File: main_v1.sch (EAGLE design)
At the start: 41 parts, among them IC1 MEGA8-P, IC2 7805TV

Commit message: Prettify
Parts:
- removed GOLD_ORB_SM2: OSHWLOGO_GOLD_ORB_MED, bfl:OSHWLOGO_GOLD_ORB_MED
- removed GOLD_ORB_SM3: OSHWLOGO_GOLD_ORB_SM, bfl:OSHWLOGO_GOLD_ORB_SM
- renumbered SV1 to H1, SV2 to H2, SV3 to H3, SV4 to H4, U$1 to IC5, U$2 to IC6, U$3 to IC4

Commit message: Added better OSHW logo
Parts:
- removed GOLD_ORB_SM1: OSHWLOGO_GOLD_ORB_LG, bfl:OSHWLOGO_GOLD_ORB_LG
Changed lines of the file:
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@@
 <part name="C8" library="adafruit" deviceset="CPOL-US" device="E2.5-5"/>
 <part name="GND22" library="supply1" deviceset="GND" device=""/>
-<part name="GOLD_ORB_SM1" library="bfl" deviceset="OSHWLOGO" device="_GOLD_ORB_LG"/>
 <part name="IC2" library="linear" deviceset="78*" device="TV" technology="05"/>
 <part name="GND9" library="supply1" deviceset="GND" device=""/>
@@
 <instance part="C8" gate="G$1" x="238.76" y="335.28"/>
 <instance part="GND22" gate="1" x="238.76" y="325.12"/>
-<instance part="GOLD_ORB_SM1" gate="G$1" x="48.26" y="73.66"/>
 <instance part="IC2" gate="A1" x="-17.78" y="88.9"/>
 <instance part="GND9" gate="1" x="-17.78" y="66.04"/>

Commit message: Prepare to move the atmega
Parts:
- added ESP8266: (no value), adafruit:PINHD-2X4
- added ICSP2: (no value), con-lstb:MA05-1
- added R13, R14, R15, R16, R17: (no value), resistor:R-EU_0204/7
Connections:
- new net N$10: ESP8266.1, ICSP2.1
- new net N$12: ESP8266.7, ICSP2.5, R17.2
- new net N$14: ESP8266.8, ICSP2.2
- new net N$17: ESP8266.3, R14.2
- new net N$19: ESP8266.5, R13.2
- new net SCL: ESP8266.4, IC1.PC5(ADC5/SCL), R16.2
- new net SDA: ESP8266.6, IC1.PC4(ADC4/SDA), ICSP2.4, R15.2
- net GND: now also ESP8266.2, ICSP2.3
- net VCC: now also R13.1, R14.1, R15.1, R16.1, R17.1
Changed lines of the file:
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@@
 <part name="R11" library="resistor" deviceset="R-EU_" device="0204/7"/>
 <part name="R12" library="resistor" deviceset="R-EU_" device="0204/7"/>
+<part name="R13" library="resistor" deviceset="R-EU_" device="0204/7"/>
+<part name="R14" library="resistor" deviceset="R-EU_" device="0204/7"/>
+<part name="R15" library="resistor" deviceset="R-EU_" device="0204/7"/>
+<part name="P+6" library="supply1" deviceset="VCC" device=""/>
+<part name="GND8" library="supply1" deviceset="GND" device=""/>
+<part name="R16" library="resistor" deviceset="R-EU_" device="0204/7"/>
+<part name="ICSP2" library="con-lstb" deviceset="MA05-1" device=""/>
+<part name="ESP8266" library="adafruit" deviceset="PINHD-2X4" device=""/>
+<part name="R17" library="resistor" deviceset="R-EU_" device="0204/7"/>
 </parts>
 <sheets>
@@
 <instance part="R11" gate="G$1" x="63.5" y="365.76" rot="R180"/>
 <instance part="R12" gate="G$1" x="63.5" y="370.84" rot="R180"/>
+<instance part="R13" gate="G$1" x="-144.78" y="294.64" rot="R270"/>
+<instance part="R14" gate="G$1" x="-137.16" y="294.64" rot="R270"/>
+<instance part="R15" gate="G$1" x="-81.28" y="294.64" rot="R270"/>
+<instance part="P+6" gate="VCC" x="-129.54" y="320.04"/>
+<instance part="GND8" gate="1" x="-114.3" y="208.28"/>
+<instance part="R16" gate="G$1" x="-86.36" y="294.64" rot="R270"/>
+<instance part="ICSP2" gate="G$1" x="-63.5" y="248.92" rot="R180"/>
+<instance part="ESP8266" gate="A" x="-116.84" y="271.78"/>
+<instance part="R17" gate="G$1" x="-129.54" y="294.64" rot="R270"/>
 </instances>
 <busses>
@@
 <wire x1="160.02" y1="88.9" x2="195.58" y2="88.9" width="0.762" layer="92"/>
 <wire x1="195.58" y1="88.9" x2="195.58" y2="233.68" width="0.762" layer="92"/>
-<wire x1="160.02" y1="88.9" x2="160.02" y2="281.94" width="0.762" layer="92"/>
+<wire x1="160.02" y1="88.9" x2="160.02" y2="236.22" width="0.762" layer="92"/>
 </segment>
 </bus>
@@
 <wire x1="38.1" y1="358.14" x2="38.1" y2="337.82" width="0.1524" layer="91"/>
 </segment>
+<segment>
+<pinref part="ICSP2" gate="G$1" pin="3"/>
+<wire x1="-71.12" y1="248.92" x2="-101.6" y2="248.92" width="0.1524" layer="91"/>
+<pinref part="GND8" gate="1" pin="GND"/>
+<wire x1="-101.6" y1="248.92" x2="-114.3" y2="248.92" width="0.1524" layer="91"/>
+<wire x1="-114.3" y1="248.92" x2="-114.3" y2="210.82" width="0.1524" layer="91"/>
+<pinref part="ESP8266" gate="A" pin="2"/>
+<wire x1="-111.76" y1="276.86" x2="-101.6" y2="276.86" width="0.1524" layer="91"/>
+<wire x1="-101.6" y1="276.86" x2="-101.6" y2="248.92" width="0.1524" layer="91"/>
+<junction x="-101.6" y="248.92"/>
+</segment>
 </net>
 <net name="VCC" class="0">
@@
 <wire x1="40.64" y1="353.06" x2="40.64" y2="365.76" width="0.1524" layer="91"/>
 <wire x1="40.64" y1="365.76" x2="17.78" y2="365.76" width="0.1524" layer="91"/>
+</segment>
+<segment>
+<pinref part="P+6" gate="VCC" pin="VCC"/>
+<pinref part="R15" gate="G$1" pin="1"/>
+<wire x1="-129.54" y1="312.42" x2="-129.54" y2="317.5" width="0.1524" layer="91"/>
+<wire x1="-81.28" y1="299.72" x2="-81.28" y2="312.42" width="0.1524" layer="91"/>
+<wire x1="-81.28" y1="312.42" x2="-86.36" y2="312.42" width="0.1524" layer="91"/>
+<pinref part="R16" gate="G$1" pin="1"/>
+<wire x1="-86.36" y1="312.42" x2="-129.54" y2="312.42" width="0.1524" layer="91"/>
+<wire x1="-86.36" y1="299.72" x2="-86.36" y2="312.42" width="0.1524" layer="91"/>
+<junction x="-86.36" y="312.42"/>
+<pinref part="R14" gate="G$1" pin="1"/>
+<wire x1="-137.16" y1="299.72" x2="-137.16" y2="312.42" width="0.1524" layer="91"/>
+<wire x1="-137.16" y1="312.42" x2="-129.54" y2="312.42" width="0.1524" layer="91"/>
+<junction x="-129.54" y="312.42"/>
+<pinref part="R13" gate="G$1" pin="1"/>
+<wire x1="-144.78" y1="299.72" x2="-144.78" y2="312.42" width="0.1524" layer="91"/>
+<wire x1="-144.78" y1="312.42" x2="-137.16" y2="312.42" width="0.1524" layer="91"/>
+<junction x="-137.16" y="312.42"/>
+<pinref part="R17" gate="G$1" pin="1"/>
+<wire x1="-129.54" y1="299.72" x2="-129.54" y2="312.42" width="0.1524" layer="91"/>
 </segment>
 </net>
@@
 </segment>
 </net>
+<net name="SCL" class="0">
+<segment>
+<pinref part="R16" gate="G$1" pin="2"/>
+<pinref part="ESP8266" gate="A" pin="4"/>
+<wire x1="-111.76" y1="274.32" x2="-86.36" y2="274.32" width="0.1524" layer="91"/>
+<wire x1="-86.36" y1="274.32" x2="-86.36" y2="289.56" width="0.1524" layer="91"/>
+<label x="-76.2" y="274.32" size="1.778" layer="95"/>
+<wire x1="-86.36" y1="274.32" x2="-78.74" y2="274.32" width="0.1524" layer="91"/>
+<junction x="-86.36" y="274.32"/>
+</segment>
+<segment>
+<pinref part="IC1" gate="G$1" pin="PC5(ADC5/SCL)"/>
+<wire x1="33.02" y1="213.36" x2="38.1" y2="213.36" width="0.1524" layer="91"/>
+<label x="38.1" y="213.36" size="1.778" layer="95"/>
+</segment>
+</net>
+<net name="N$10" class="0">
+<segment>
+<pinref part="ESP8266" gate="A" pin="1"/>
+<wire x1="-119.38" y1="276.86" x2="-132.08" y2="276.86" width="0.1524" layer="91"/>
+<pinref part="ICSP2" gate="G$1" pin="1"/>
+<wire x1="-132.08" y1="276.86" x2="-132.08" y2="254" width="0.1524" layer="91"/>
+<wire x1="-132.08" y1="254" x2="-71.12" y2="254" width="0.1524" layer="91"/>
+</segment>
+</net>
+<net name="N$14" class="0">
+<segment>
+<pinref part="ESP8266" gate="A" pin="8"/>
+<wire x1="-111.76" y1="269.24" x2="-99.06" y2="269.24" width="0.1524" layer="91"/>
+<pinref part="ICSP2" gate="G$1" pin="2"/>
+<wire x1="-99.06" y1="269.24" x2="-99.06" y2="251.46" width="0.1524" layer="91"/>
+<wire x1="-99.06" y1="251.46" x2="-71.12" y2="251.46" width="0.1524" layer="91"/>
+</segment>
+</net>
+<net name="N$17" class="0">
+<segment>
+<pinref part="ESP8266" gate="A" pin="3"/>
+<pinref part="R14" gate="G$1" pin="2"/>
+<wire x1="-119.38" y1="274.32" x2="-137.16" y2="274.32" width="0.1524" layer="91"/>
+<wire x1="-137.16" y1="274.32" x2="-137.16" y2="289.56" width="0.1524" layer="91"/>
+</segment>
+</net>
+<net name="N$19" class="0">
+<segment>
+<pinref part="ESP8266" gate="A" pin="5"/>
+<pinref part="R13" gate="G$1" pin="2"/>
+<wire x1="-119.38" y1="271.78" x2="-144.78" y2="271.78" width="0.1524" layer="91"/>
+<wire x1="-144.78" y1="271.78" x2="-144.78" y2="289.56" width="0.1524" layer="91"/>
+</segment>
+</net>
+<net name="SDA" class="0">
+<segment>
+<pinref part="R15" gate="G$1" pin="2"/>
+<pinref part="ESP8266" gate="A" pin="6"/>
+<wire x1="-81.28" y1="289.56" x2="-81.28" y2="271.78" width="0.1524" layer="91"/>
+<wire x1="-81.28" y1="271.78" x2="-96.52" y2="271.78" width="0.1524" layer="91"/>
+<wire x1="-96.52" y1="271.78" x2="-111.76" y2="271.78" width="0.1524" layer="91"/>
+<junction x="-96.52" y="271.78"/>
+<label x="-76.2" y="271.78" size="1.778" layer="95"/>
+<wire x1="-96.52" y1="246.38" x2="-96.52" y2="271.78" width="0.1524" layer="91"/>
+<wire x1="-81.28" y1="271.78" x2="-78.74" y2="271.78" width="0.1524" layer="91"/>
+<junction x="-81.28" y="271.78"/>
+<pinref part="ICSP2" gate="G$1" pin="4"/>
+<wire x1="-71.12" y1="246.38" x2="-96.52" y2="246.38" width="0.1524" layer="91"/>
+</segment>
+<segment>
+<pinref part="IC1" gate="G$1" pin="PC4(ADC4/SDA)"/>
+<wire x1="33.02" y1="215.9" x2="38.1" y2="215.9" width="0.1524" layer="91"/>
+<label x="38.1" y="215.9" size="1.778" layer="95"/>
+</segment>
+</net>
+<net name="N$12" class="0">
+<segment>
+<pinref part="ESP8266" gate="A" pin="7"/>
+<wire x1="-119.38" y1="269.24" x2="-129.54" y2="269.24" width="0.1524" layer="91"/>
+<wire x1="-129.54" y1="243.84" x2="-129.54" y2="269.24" width="0.1524" layer="91"/>
+<pinref part="R17" gate="G$1" pin="2"/>
+<wire x1="-129.54" y1="289.56" x2="-129.54" y2="269.24" width="0.1524" layer="91"/>
+<junction x="-129.54" y="269.24"/>
+<pinref part="ICSP2" gate="G$1" pin="5"/>
+<wire x1="-71.12" y1="243.84" x2="-129.54" y2="243.84" width="0.1524" layer="91"/>
+</segment>
+</net>

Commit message: Move ESP ICSP header, and bits into the board
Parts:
- R13, R15, R17: device resistor:R-EU_0204/7 -> resistor:R-EU_0204/2V
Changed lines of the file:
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@@
 <part name="R11" library="resistor" deviceset="R-EU_" device="0204/7"/>
 <part name="R12" library="resistor" deviceset="R-EU_" device="0204/7"/>
-<part name="R13" library="resistor" deviceset="R-EU_" device="0204/7"/>
+<part name="R13" library="resistor" deviceset="R-EU_" device="0204/2V"/>
 <part name="R14" library="resistor" deviceset="R-EU_" device="0204/7"/>
-<part name="R15" library="resistor" deviceset="R-EU_" device="0204/7"/>
+<part name="R15" library="resistor" deviceset="R-EU_" device="0204/2V"/>
 <part name="P+6" library="supply1" deviceset="VCC" device=""/>
 <part name="GND8" library="supply1" deviceset="GND" device=""/>
@@
 <part name="ICSP2" library="con-lstb" deviceset="MA05-1" device=""/>
 <part name="ESP8266" library="adafruit" deviceset="PINHD-2X4" device=""/>
-<part name="R17" library="resistor" deviceset="R-EU_" device="0204/7"/>
+<part name="R17" library="resistor" deviceset="R-EU_" device="0204/2V"/>
 </parts>
 <sheets>

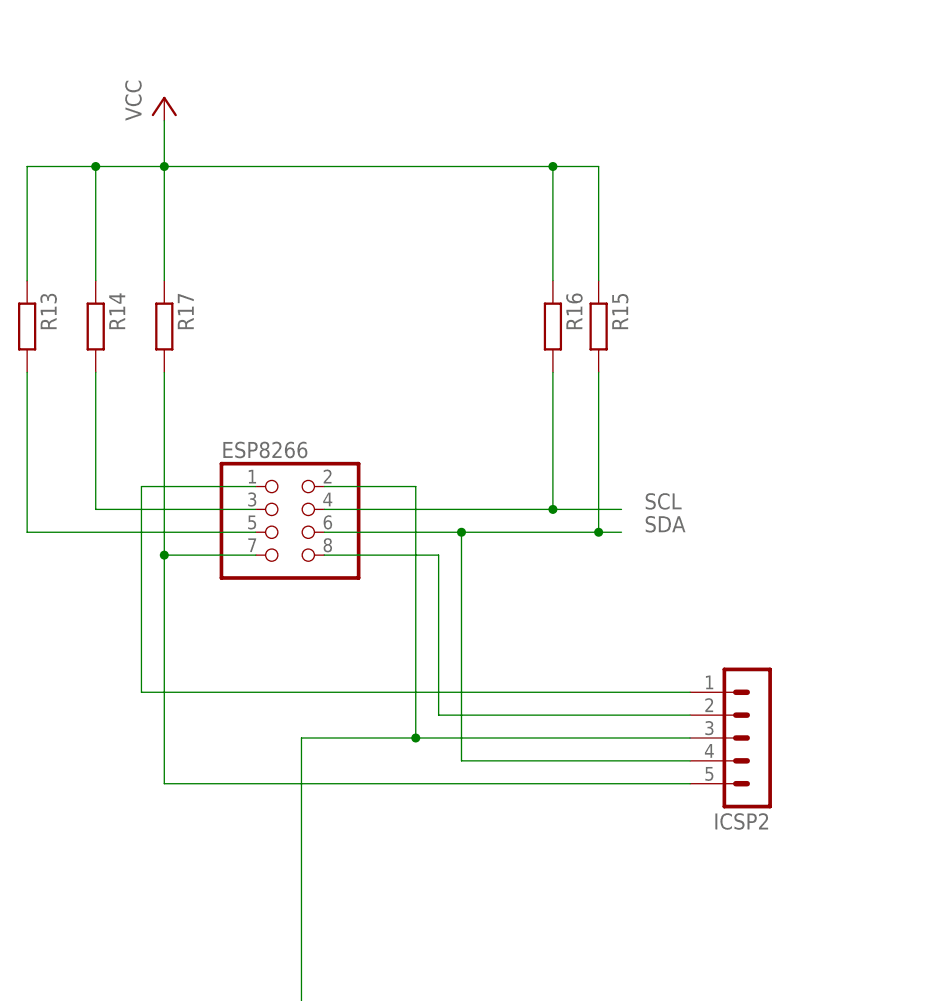
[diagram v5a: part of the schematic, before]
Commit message: Fix ESP socket connections
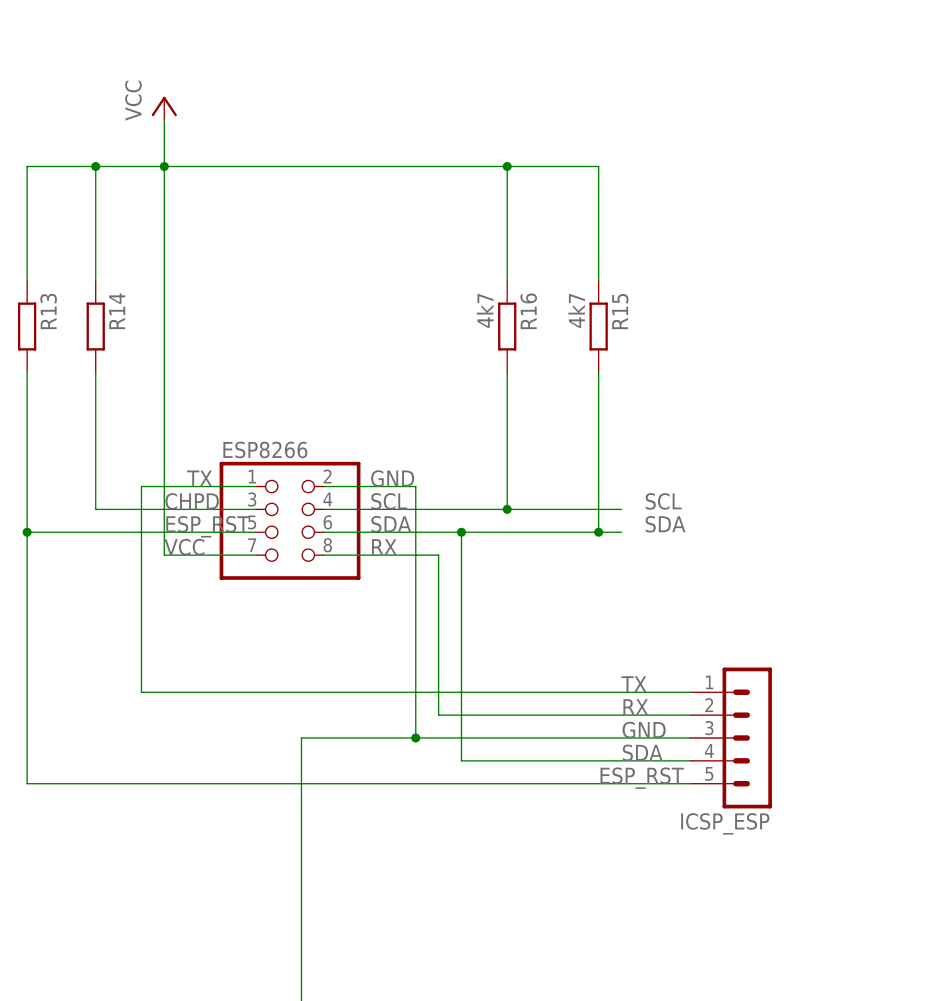
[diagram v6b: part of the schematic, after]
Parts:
- removed R17: (no value), resistor:R-EU_0204/2V
- R15: value (none) -> 4k7; device resistor:R-EU_0204/2V -> resistor:R-EU_0204/7
- R16: value (none) -> 4k7
- renumbered ICSP2 to ICSP_ESP
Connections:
- net N$10 renamed TX
- net N$14 renamed RX
- net N$17 renamed CHPD
- removed net N$12: ESP8266.7, ICSP_ESP.5, R17.2
- removed net N$19: ESP8266.5, R13.2
- new net ESP_RST: ESP8266.5, ICSP_ESP.5, R13.2
- net VCC: now also ESP8266.7; no longer R17.1
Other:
- moved on the sheet: R16
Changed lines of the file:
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@@
 <part name="R13" library="resistor" deviceset="R-EU_" device="0204/2V"/>
 <part name="R14" library="resistor" deviceset="R-EU_" device="0204/7"/>
-<part name="R15" library="resistor" deviceset="R-EU_" device="0204/2V"/>
+<part name="R15" library="resistor" deviceset="R-EU_" device="0204/7" value="4k7"/>
 <part name="P+6" library="supply1" deviceset="VCC" device=""/>
 <part name="GND8" library="supply1" deviceset="GND" device=""/>
-<part name="R16" library="resistor" deviceset="R-EU_" device="0204/7"/>
-<part name="ICSP2" library="con-lstb" deviceset="MA05-1" device=""/>
+<part name="R16" library="resistor" deviceset="R-EU_" device="0204/7" value="4k7"/>
+<part name="ICSP_ESP" library="con-lstb" deviceset="MA05-1" device=""/>
 <part name="ESP8266" library="adafruit" deviceset="PINHD-2X4" device=""/>
-<part name="R17" library="resistor" deviceset="R-EU_" device="0204/2V"/>
 </parts>
 <sheets>
@@
 <instance part="P+6" gate="VCC" x="-129.54" y="320.04"/>
 <instance part="GND8" gate="1" x="-114.3" y="208.28"/>
-<instance part="R16" gate="G$1" x="-86.36" y="294.64" rot="R270"/>
-<instance part="ICSP2" gate="G$1" x="-63.5" y="248.92" rot="R180"/>
+<instance part="R16" gate="G$1" x="-91.44" y="294.64" rot="R270"/>
+<instance part="ICSP_ESP" gate="G$1" x="-63.5" y="248.92" rot="R180"/>
 <instance part="ESP8266" gate="A" x="-116.84" y="271.78"/>
-<instance part="R17" gate="G$1" x="-129.54" y="294.64" rot="R270"/>
 </instances>
 <busses>
@@
 </segment>
 <segment>
-<pinref part="ICSP2" gate="G$1" pin="3"/>
+<pinref part="ICSP_ESP" gate="G$1" pin="3"/>
 <wire x1="-71.12" y1="248.92" x2="-101.6" y2="248.92" width="0.1524" layer="91"/>
 <pinref part="GND8" gate="1" pin="GND"/>
@@
 <wire x1="-101.6" y1="276.86" x2="-101.6" y2="248.92" width="0.1524" layer="91"/>
 <junction x="-101.6" y="248.92"/>
+<label x="-78.74" y="248.92" size="1.778" layer="95"/>
+<label x="-106.68" y="276.86" size="1.778" layer="95"/>
 </segment>
 </net>
@@
 <wire x1="-129.54" y1="312.42" x2="-129.54" y2="317.5" width="0.1524" layer="91"/>
 <wire x1="-81.28" y1="299.72" x2="-81.28" y2="312.42" width="0.1524" layer="91"/>
-<wire x1="-81.28" y1="312.42" x2="-86.36" y2="312.42" width="0.1524" layer="91"/>
+<wire x1="-81.28" y1="312.42" x2="-91.44" y2="312.42" width="0.1524" layer="91"/>
 <pinref part="R16" gate="G$1" pin="1"/>
-<wire x1="-86.36" y1="312.42" x2="-129.54" y2="312.42" width="0.1524" layer="91"/>
-<wire x1="-86.36" y1="299.72" x2="-86.36" y2="312.42" width="0.1524" layer="91"/>
-<junction x="-86.36" y="312.42"/>
+<wire x1="-91.44" y1="312.42" x2="-129.54" y2="312.42" width="0.1524" layer="91"/>
+<wire x1="-91.44" y1="299.72" x2="-91.44" y2="312.42" width="0.1524" layer="91"/>
+<junction x="-91.44" y="312.42"/>
 <pinref part="R14" gate="G$1" pin="1"/>
 <wire x1="-137.16" y1="299.72" x2="-137.16" y2="312.42" width="0.1524" layer="91"/>
@@
 <wire x1="-144.78" y1="312.42" x2="-137.16" y2="312.42" width="0.1524" layer="91"/>
 <junction x="-137.16" y="312.42"/>
-<pinref part="R17" gate="G$1" pin="1"/>
-<wire x1="-129.54" y1="299.72" x2="-129.54" y2="312.42" width="0.1524" layer="91"/>
+<pinref part="ESP8266" gate="A" pin="7"/>
+<wire x1="-129.54" y1="312.42" x2="-129.54" y2="269.24" width="0.1524" layer="91"/>
+<wire x1="-129.54" y1="269.24" x2="-119.38" y2="269.24" width="0.1524" layer="91"/>
+<label x="-129.54" y="269.24" size="1.778" layer="95"/>
 </segment>
 </net>
@@
 <pinref part="R16" gate="G$1" pin="2"/>
 <pinref part="ESP8266" gate="A" pin="4"/>
-<wire x1="-111.76" y1="274.32" x2="-86.36" y2="274.32" width="0.1524" layer="91"/>
-<wire x1="-86.36" y1="274.32" x2="-86.36" y2="289.56" width="0.1524" layer="91"/>
+<wire x1="-111.76" y1="274.32" x2="-91.44" y2="274.32" width="0.1524" layer="91"/>
+<wire x1="-91.44" y1="274.32" x2="-91.44" y2="289.56" width="0.1524" layer="91"/>
 <label x="-76.2" y="274.32" size="1.778" layer="95"/>
-<wire x1="-86.36" y1="274.32" x2="-78.74" y2="274.32" width="0.1524" layer="91"/>
-<junction x="-86.36" y="274.32"/>
+<wire x1="-91.44" y1="274.32" x2="-78.74" y2="274.32" width="0.1524" layer="91"/>
+<junction x="-91.44" y="274.32"/>
+<label x="-106.68" y="274.32" size="1.778" layer="95"/>
 </segment>
 <segment>
@@
 </segment>
 </net>
-<net name="N$10" class="0">
+<net name="TX" class="0">
 <segment>
 <pinref part="ESP8266" gate="A" pin="1"/>
 <wire x1="-119.38" y1="276.86" x2="-132.08" y2="276.86" width="0.1524" layer="91"/>
-<pinref part="ICSP2" gate="G$1" pin="1"/>
+<pinref part="ICSP_ESP" gate="G$1" pin="1"/>
 <wire x1="-132.08" y1="276.86" x2="-132.08" y2="254" width="0.1524" layer="91"/>
 <wire x1="-132.08" y1="254" x2="-71.12" y2="254" width="0.1524" layer="91"/>
-</segment>
-</net>
-<net name="N$14" class="0">
+<label x="-78.74" y="254" size="1.778" layer="95"/>
+<label x="-127" y="276.86" size="1.778" layer="95"/>
+</segment>
+</net>
+<net name="RX" class="0">
 <segment>
 <pinref part="ESP8266" gate="A" pin="8"/>
 <wire x1="-111.76" y1="269.24" x2="-99.06" y2="269.24" width="0.1524" layer="91"/>
-<pinref part="ICSP2" gate="G$1" pin="2"/>
+<pinref part="ICSP_ESP" gate="G$1" pin="2"/>
 <wire x1="-99.06" y1="269.24" x2="-99.06" y2="251.46" width="0.1524" layer="91"/>
 <wire x1="-99.06" y1="251.46" x2="-71.12" y2="251.46" width="0.1524" layer="91"/>
-</segment>
-</net>
-<net name="N$17" class="0">
+<label x="-78.74" y="251.46" size="1.778" layer="95"/>
+<label x="-106.68" y="269.24" size="1.778" layer="95"/>
+</segment>
+</net>
+<net name="CHPD" class="0">
 <segment>
 <pinref part="ESP8266" gate="A" pin="3"/>
@@
 <wire x1="-119.38" y1="274.32" x2="-137.16" y2="274.32" width="0.1524" layer="91"/>
 <wire x1="-137.16" y1="274.32" x2="-137.16" y2="289.56" width="0.1524" layer="91"/>
-</segment>
-</net>
-<net name="N$19" class="0">
-<segment>
-<pinref part="ESP8266" gate="A" pin="5"/>
-<pinref part="R13" gate="G$1" pin="2"/>
-<wire x1="-119.38" y1="271.78" x2="-144.78" y2="271.78" width="0.1524" layer="91"/>
-<wire x1="-144.78" y1="271.78" x2="-144.78" y2="289.56" width="0.1524" layer="91"/>
+<label x="-129.54" y="274.32" size="1.778" layer="95"/>
 </segment>
 </net>
@@
 <wire x1="-81.28" y1="271.78" x2="-78.74" y2="271.78" width="0.1524" layer="91"/>
 <junction x="-81.28" y="271.78"/>
-<pinref part="ICSP2" gate="G$1" pin="4"/>
+<pinref part="ICSP_ESP" gate="G$1" pin="4"/>
 <wire x1="-71.12" y1="246.38" x2="-96.52" y2="246.38" width="0.1524" layer="91"/>
+<label x="-78.74" y="246.38" size="1.778" layer="95"/>
+<label x="-106.68" y="271.78" size="1.778" layer="95"/>
 </segment>
 <segment>
@@
 </segment>
 </net>
-<net name="N$12" class="0">
-<segment>
-<pinref part="ESP8266" gate="A" pin="7"/>
-<wire x1="-119.38" y1="269.24" x2="-129.54" y2="269.24" width="0.1524" layer="91"/>
-<wire x1="-129.54" y1="243.84" x2="-129.54" y2="269.24" width="0.1524" layer="91"/>
-<pinref part="R17" gate="G$1" pin="2"/>
-<wire x1="-129.54" y1="289.56" x2="-129.54" y2="269.24" width="0.1524" layer="91"/>
-<junction x="-129.54" y="269.24"/>
-<pinref part="ICSP2" gate="G$1" pin="5"/>
-<wire x1="-71.12" y1="243.84" x2="-129.54" y2="243.84" width="0.1524" layer="91"/>
-</segment>
-</net>
+<net name="ESP_RST" class="0">
+<segment>
+<pinref part="ICSP_ESP" gate="G$1" pin="5"/>
+<wire x1="-71.12" y1="243.84" x2="-144.78" y2="243.84" width="0.1524" layer="91"/>
+<label x="-81.28" y="243.84" size="1.778" layer="95"/>
+<pinref part="R13" gate="G$1" pin="2"/>
+<wire x1="-144.78" y1="271.78" x2="-144.78" y2="289.56" width="0.1524" layer="91"/>
+<pinref part="ESP8266" gate="A" pin="5"/>
+<wire x1="-119.38" y1="271.78" x2="-144.78" y2="271.78" width="0.1524" layer="91"/>
+<wire x1="-144.78" y1="271.78" x2="-144.78" y2="243.84" width="0.1524" layer="91"/>
+<junction x="-144.78" y="271.78"/>
+<label x="-129.54" y="271.78" size="1.778" layer="95"/>
+</segment>
+</net>
